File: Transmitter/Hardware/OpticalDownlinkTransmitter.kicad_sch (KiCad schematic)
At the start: 34 parts, among them J1 Conn_01x04_Pin, J2 Conn_01x04_Pin, U1 AL8860MP, U2 AL8860MP, U3 AL8860MP, U4 AL8860MP

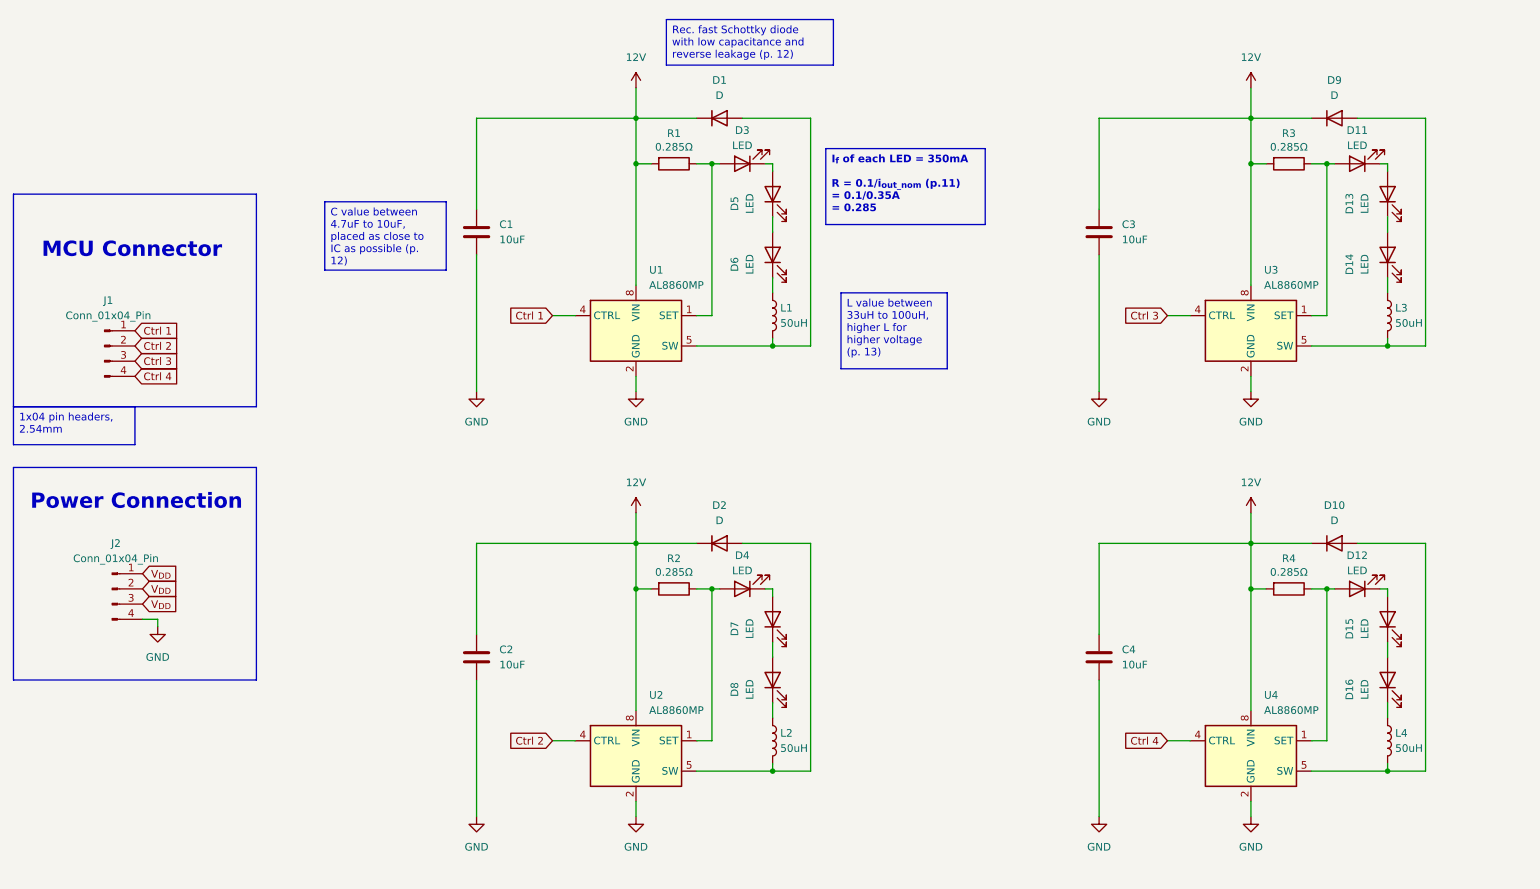
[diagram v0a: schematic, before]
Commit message: Added capacitors and fixed values in schematic
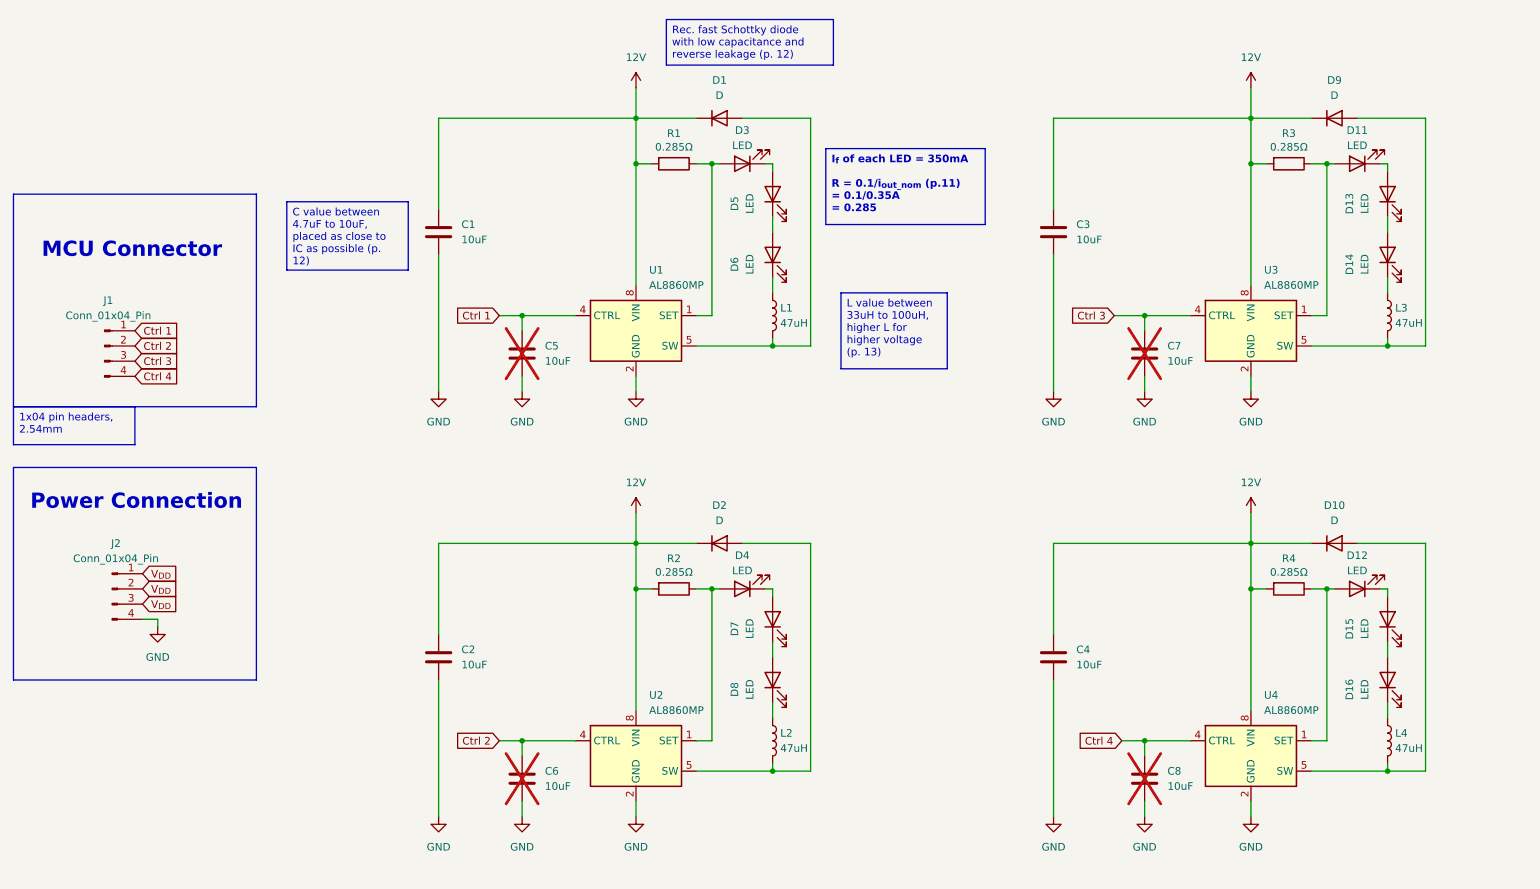
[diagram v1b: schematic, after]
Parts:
- added C5, C6, C7, C8: 10uF, Capacitor_SMD:C_0805_2012Metric_Pad1.18x1.45mm_HandSolder, symbol Device:C
- L1, L2, L3, L4: value 50uH -> 47uH
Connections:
- net Ctrl 1: now also C5.1
- net Ctrl 2: now also C6.1
- net Ctrl 3: now also C7.1
- net Ctrl 4: now also C8.1
- net GND: now also C5.2, C6.2, C7.2, C8.2
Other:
- moved on the sheet: C1, C2, C3, C4

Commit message: Added extra connectors and changed resistor
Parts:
- added J3, J4: Conn_01x04, symbol Connector_Generic:Conn_01x04
- R1, R2, R3, R4: value 0.285Ω -> 0.250Ω; footprint Resistor_SMD:R_0805_2012Metric_Pad1.20x1.40mm_HandSolder -> Resistor_SMD:R_2512_6332Metric_Pad1.40x3.35mm_HandSolder; JLCPCB Part C20485079 -> C875877
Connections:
- net Ctrl 1: now also J3.1 (Pin_1)
- net Ctrl 2: now also J3.2 (Pin_2)
- net Ctrl 3: now also J3.3 (Pin_3)
- net Ctrl 4: now also J3.4 (Pin_4)
- net GND: now also J4.4 (Pin_4)
- net V_{DD}: now also J4.1 (Pin_1), J4.2 (Pin_2), J4.3 (Pin_3)
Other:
- moved on the sheet: C1, C2, C3, C4, C5, C6, C7, C8, D1, D10, D11, D12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

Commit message: added footprints and redid layout
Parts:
- D1, D10, D2, D9: footprint Footprint Library:P2_DO-201 -> Footprint Library:DIOM7959X261N; JLCPCB Part C5357977 -> C236151
- J3, J4: footprint (none) -> Footprint Library:CONN_532610001-SD_04_MOL
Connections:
- net Ctrl 1: now also J3.4 (Pin_4); no longer J3.1 (Pin_1)
- net Ctrl 2: now also J3.3 (Pin_3); no longer J3.2 (Pin_2)
- net Ctrl 3: now also J3.2 (Pin_2); no longer J3.3 (Pin_3)
- net Ctrl 4: now also J3.1 (Pin_1); no longer J3.4 (Pin_4)
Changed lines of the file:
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@@
 	(text_box "I_{f} of each LED = 350mA\n\nR = 0.1/i_{out_nom} (p.11)\n  = 0.1/0.35A \n  = 0.285 "
 		(exclude_from_sim no)
-		(at 175.26 41.91 0)
+		(at 175.26 45.72 0)
 		(size 26.67 12.7)
 		(margins 0.9525 0.9525 0.9525 0.9525)
@@
 	(text_box "Rec. fast Schottky diode with low capacitance and reverse leakage (p. 12)"
 		(exclude_from_sim no)
-		(at 148.59 20.32 0)
+		(at 175.26 34.29 0)
 		(size 27.94 7.62)
 		(margins 0.9525 0.9525 0.9525 0.9525)
@@
 	(text_box "L value between 33uH to 100uH, higher L for higher voltage (p. 13)"
 		(exclude_from_sim no)
-		(at 177.8 66.04 0)
+		(at 175.26 62.23 0)
 		(size 17.78 12.7)
 		(margins 0.9525 0.9525 0.9525 0.9525)
@@
 	(text_box "C value between 4.7uF to 10uF, placed as close to IC as possible (p. 12)"
 		(exclude_from_sim no)
-		(at 85.09 50.8 0)
+		(at 85.09 36.83 0)
 		(size 20.32 11.43)
 		(margins 0.9525 0.9525 0.9525 0.9525)
@@
 	(global_label "Ctrl 2"
 		(shape input)
-		(at 41.91 81.28 180)
+		(at 41.91 83.82 180)
 		(fields_autoplaced yes)
 		(effects
@@
 		)
 		(property "Intersheetrefs" "${INTERSHEET_REFS}"
-			(at 33.3006 81.28 0)
+			(at 33.3006 83.82 0)
 			(effects
 				(font
@@
 	(global_label "Ctrl 1"
 		(shape input)
-		(at 41.91 78.74 180)
+		(at 41.91 86.36 180)
 		(fields_autoplaced yes)
 		(effects
@@
 		)
 		(property "Intersheetrefs" "${INTERSHEET_REFS}"
-			(at 33.3006 78.74 0)
+			(at 33.3006 86.36 0)
 			(effects
 				(font
@@
 	(global_label "Ctrl 3"
 		(shape input)
-		(at 41.91 83.82 180)
+		(at 41.91 81.28 180)
 		(fields_autoplaced yes)
 		(effects
@@
 		)
 		(property "Intersheetrefs" "${INTERSHEET_REFS}"
-			(at 33.3006 83.82 0)
+			(at 33.3006 81.28 0)
 			(effects
 				(font
@@
 	(global_label "Ctrl 4"
 		(shape input)
-		(at 41.91 86.36 180)
+		(at 41.91 78.74 180)
 		(fields_autoplaced yes)
 		(effects
@@
 		)
 		(property "Intersheetrefs" "${INTERSHEET_REFS}"
-			(at 33.3006 86.36 0)
+			(at 33.3006 78.74 0)
 			(effects
 				(font
@@
 			)
 		)
-		(property "Footprint" "Footprint Library:P2_DO-201"
+		(property "Footprint" "Footprint Library:DIOM7959X261N"
 			(at 260.35 107.95 0)
 			(effects
@@
 			)
 		)
-		(property "JLCPCB Part" "C5357977"
+		(property "JLCPCB Part" "C236151"
 			(at 260.35 107.95 0)
 			(effects
@@
 			)
 		)
-		(property "Footprint" ""
+		(property "Footprint" "Footprint Library:CONN_532610001-SD_04_MOL"
 			(at 46.99 81.28 0)
 			(effects
@@
 			)
 		)
-		(property "Footprint" "Footprint Library:P2_DO-201"
+		(property "Footprint" "Footprint Library:DIOM7959X261N"
 			(at 157.48 107.95 0)
 			(effects
@@
 			)
 		)
-		(property "JLCPCB Part" "C5357977"
+		(property "JLCPCB Part" "C236151"
 			(at 157.48 107.95 0)
 			(effects
@@
 			)
 		)
-		(property "Footprint" ""
+		(property "Footprint" "Footprint Library:CONN_532610001-SD_04_MOL"
 			(at 45.72 149.86 0)
 			(effects
@@
 			)
 		)
-		(property "Footprint" "Footprint Library:P2_DO-201"
+		(property "Footprint" "Footprint Library:DIOM7959X261N"
 			(at 260.35 36.83 0)
 			(effects
@@
 			)
 		)
-		(property "JLCPCB Part" "C5357977"
+		(property "JLCPCB Part" "C236151"
 			(at 260.35 36.83 0)
 			(effects
@@
 			)
 		)
-		(property "Footprint" "Footprint Library:P2_DO-201"
+		(property "Footprint" "Footprint Library:DIOM7959X261N"
 			(at 157.48 36.83 0)
 			(effects
@@
 			)
 		)
-		(property "JLCPCB Part" "C5357977"
+		(property "JLCPCB Part" "C236151"
 			(at 157.48 36.83 0)
 			(effects

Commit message: Adjusted layout so tracing would be easier
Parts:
- D1, D10, D2, D9: footprint Footprint Library:DIOM7959X261N -> Footprint Library:DIOM7958X256N
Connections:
- net V_{DD} is gone; now on net 12V: J2.1 (Pin_1), J2.2 (Pin_2), J2.3 (Pin_3), J4.1 (Pin_1), J4.2 (Pin_2), J4.3 (Pin_3)
- net 12V: now also D1.2 (A); no longer D1.1 (K)
- net at L1.2, U1.5 (SW), U1.6 (SW): now also D1.1 (K); no longer D1.2 (A)

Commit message: completed tracing and changed polygon clearance and fixed up math in schematic
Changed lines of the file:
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@@
 		)
 	)
-	(text_box "R value chosen to accomadate for 0.074Ω resistance from the inductor\n\ni = 0.4A for R = 0.250Ω\ni = 3.086A for R = 0.20Ω + 0.074Ω = 0.324Ω"
+	(text_box "R value chosen to accomadate for 0.074Ω resistance from the inductor using same formula on p. 11\n\ni = 0.4A for R = 0.250Ω\ni = 0.3086A for R = 0.250Ω + 0.074Ω = 0.324Ω"
 		(exclude_from_sim no)
 		(at 85.09 21.59 0)
-		(size 49.53 11.43)
+		(size 54.61 11.43)
 		(margins 0.9525 0.9525 0.9525 0.9525)
 		(stroke
